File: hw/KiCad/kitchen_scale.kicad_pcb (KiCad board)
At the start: 2 copper layers, 59 x 50 mm, 11 parts, among them J1 Conn_01x08_Socket, J2 Conn_HX711, SW1 SW_Push, SW2 SW_SPST, SW3 SW_Push, SW4 SW_Push, U1 DEBO1_3_7LI_1_0A charge_contr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, U2 WeMos_D1_mini, U3 LF33_TO220

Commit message: Update of fine placement
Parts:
- moved R1 5.59 mm to (82.7, 83.0)
- moved SW1 1.00 mm to (66.8, 115.5)
- moved SW3 1.00 mm to (83.8, 115.5)
- moved SW4 1.00 mm to (100.8, 115.5)
- moved U2 1.00 mm to (116.9, 102.0)
- moved J2 0.80 mm to (79.0, 77.0)
- moved J1 0.50 mm to (64.0, 79.5)
- moved U1 0.50 mm to (60.8, 92.5)
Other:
- board size 59 x 50 mm -> 60 x 50 mm
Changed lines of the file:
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@@
   (net 22 "unconnected-(U2-TX-Pad16)")
   (footprint "Button_Switch_THT:SW_PUSH-12mm" (layer "F.Cu")
-    (at 65.76 115.5)
+    (at 66.76 115.5)
     (descr "SW PUSH 12mm https://www.e-switch.com/system/asset/product_line/data_sheet/143/TL1100.pdf")
     (tags "tact sw push 12mm")
@@
   )
   (footprint "Connector_PinSocket_2.54mm:PinSocket_1x04_P2.54mm_Vertical" (layer "F.Cu")
-    (at 78.2 76.975 90)
+    (at 79 76.975 90)
     (descr "Through hole straight socket strip, 1x04, 2.54mm pitch, single row (from Kicad 4.0.7), script generated")
     (tags "Through hole socket strip THT 1x04 2.54mm single row")
@@
   )
   (footprint "Button_Switch_THT:SW_PUSH-12mm" (layer "F.Cu")
-    (at 82.76 115.5)
+    (at 83.76 115.5)
     (descr "SW PUSH 12mm https://www.e-switch.com/system/asset/product_line/data_sheet/143/TL1100.pdf")
     (tags "tact sw push 12mm")
@@
   )
   (footprint "Resistor_THT:R_Axial_DIN0207_L6.3mm_D2.5mm_P7.62mm_Horizontal" (layer "F.Cu")
-    (at 77.19 82)
+    (at 82.69 83)
     (descr "Resistor, Axial_DIN0207 series, Axial, Horizontal, pin pitch=7.62mm, 0.25W = 1/4W, length*diameter=6.3*2.5mm^2, http://cdn-reichelt.de/documents/datenblatt/B400/1_4W%23YAG.pdf")
     (tags "Resistor Axial_DIN0207 series Axial Horizontal pin pitch 7.62mm 0.25W = 1/4W length 6.3mm diameter 2.5mm")
@@
   )
   (footprint "Mine:DEBO1_3_7LI_1_0A_charge_controller" (layer "F.Cu")
-    (at 61.3 92.5)
+    (at 60.8 92.5)
     (descr "Texas Instruments EUS 5 Pin Double Sided Module")
     (tags "module pcb")
@@
   )
   (footprint "Module:WEMOS_D1_mini_light" (layer "F.Cu")
-    (at 115.86 102 180)
+    (at 116.86 102 180)
     (descr "16-pin module, column spacing 22.86 mm (900 mils), https://wiki.wemos.cc/products:d1:d1_mini, https://c1.staticflickr.com/1/734/31400410271_f278b087db_z.jpg")
     (tags "ESP8266 WiFi microcontroller")
@@
   )
   (footprint "Connector_PinHeader_2.54mm:PinHeader_2x04_P2.54mm_Vertical" (layer "F.Cu")
-    (at 64.46 79.54 90)
+    (at 63.96 79.5 90)
     (descr "Through hole straight pin header, 2x04, 2.54mm pitch, double rows")
     (tags "Through hole pin header THT 2x04 2.54mm double row")
@@
   )
   (footprint "Button_Switch_THT:SW_PUSH-12mm" (layer "F.Cu")
-    (at 99.76 115.5)
+    (at 100.76 115.5)
     (descr "SW PUSH 12mm https://www.e-switch.com/system/asset/product_line/data_sheet/143/TL1100.pdf")
     (tags "tact sw push 12mm")
@@
     )
   )
-  (gr_rect (start 60 75) (end 119 125)
+  (gr_rect (start 60 75) (end 120 125)
     (stroke (width 0.1) (type default)) (fill none) (layer "Edge.Cuts"))
 )

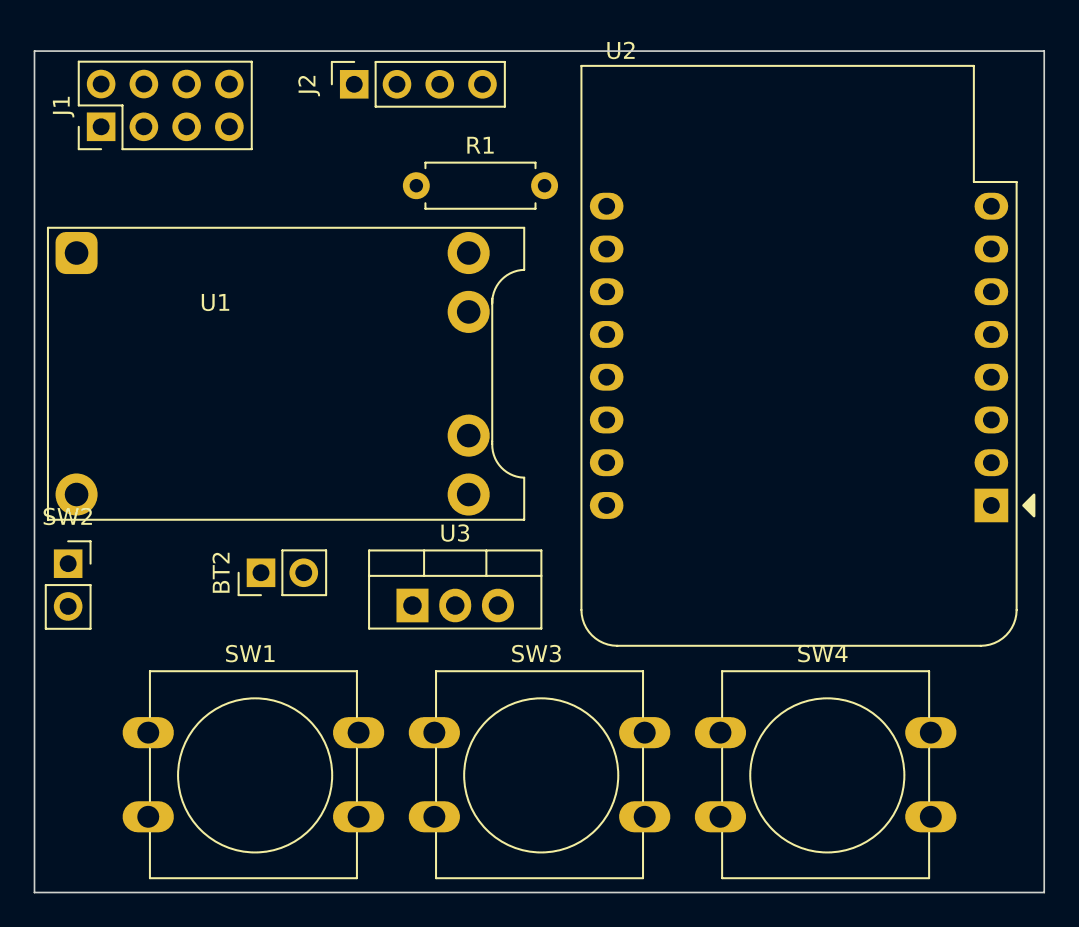
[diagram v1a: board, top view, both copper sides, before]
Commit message: Completed wiring
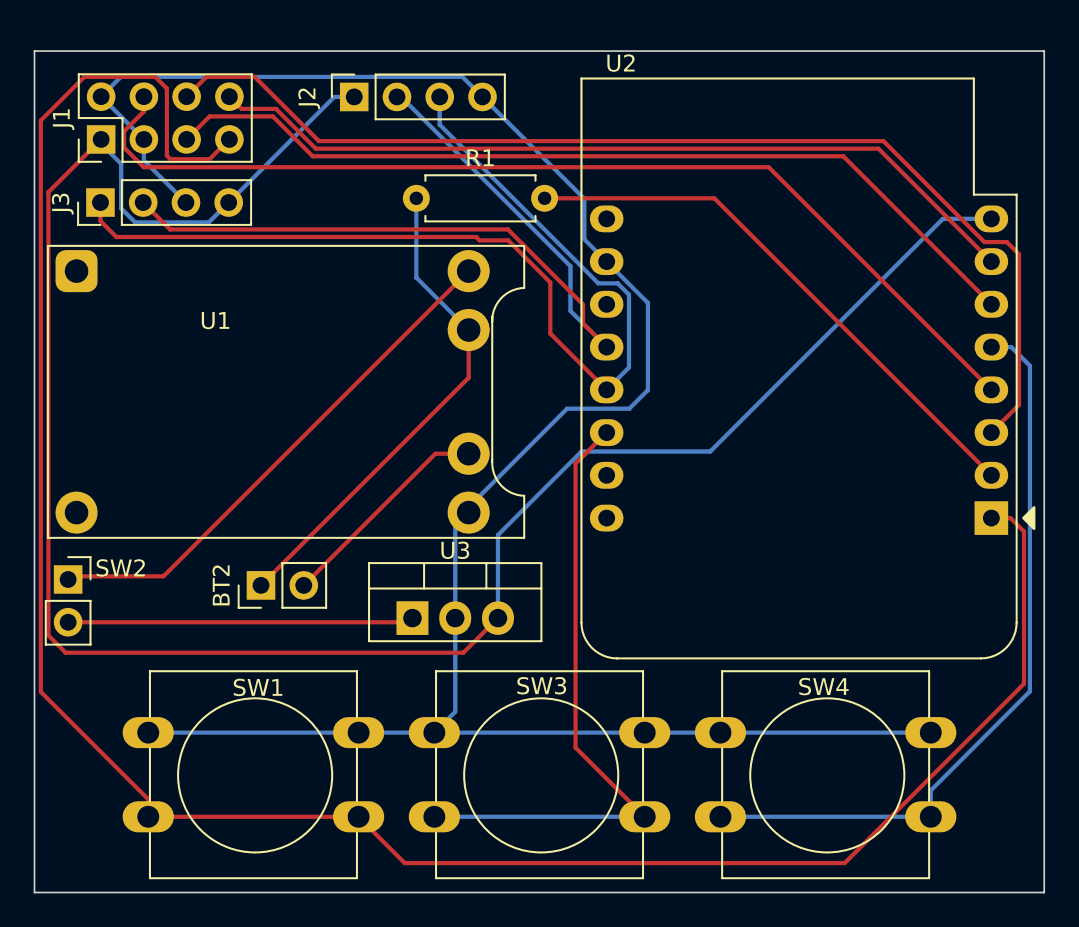
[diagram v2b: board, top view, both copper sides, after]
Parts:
- added J3: Conn_01x04_Pin, Connector_PinHeader_2.54mm:PinHeader_1x04_P2.54mm_Vertical, F.Cu at (63.9, 84.0)
- moved U1 1.08 mm to (60.8, 93.6)
- moved SW2 0.94 mm to (62.0, 106.4)
- moved BT2 0.75 mm to (73.5, 106.8)
- moved J1 0.75 mm to (64.0, 80.2)
- moved J2 0.75 mm to (79.0, 77.7)
- moved R1 0.75 mm to (82.7, 83.8)
- moved U2 0.75 mm to (116.9, 102.8)
- moved U3 0.75 mm to (82.5, 108.7)
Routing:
- net /~{RESET}: track 0.00 -> 130.1 mm
- net GND: track 0.00 -> 128.5 mm
- net +3.3V: track 0.00 -> 122.7 mm
- net /TFT_RS: track 0.00 -> 65.6 mm
- net /SPI_SCK: track 0.00 -> 61.0 mm
- net /D2_DT: track 0.00 -> 60.4 mm
- net /SPI_COPI: track 0.00 -> 53.0 mm
- net /D3_SCK: track 0.00 -> 51.9 mm
- net /SPI_CS: track 0.00 -> 49.3 mm
- net /BTN_2ND: track 0.00 -> 44.5 mm
- net /BTN_TARE: track 0.00 -> 37.8 mm
- net Net-(U2-A0): track 0.00 -> 33.4 mm
- net Net-(SW2-A): track 0.00 -> 31.7 mm
- net +BATT: track 0.00 -> 29.4 mm
- net Net-(SW2-B): track 0.00 -> 20.8 mm
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
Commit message: Add label
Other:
- board text added: "Kitchen Scale 2.0 egsoft, 2025"
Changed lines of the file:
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@@
   (gr_rect (start 60 75) (end 120 125)
     (stroke (width 0.1) (type default)) (fill none) (layer "Edge.Cuts"))
+  (gr_text "Kitchen Scale 2.0\negsoft, 2025" (at 63.15 95.35) (layer "F.SilkS")
+    (effects (font (size 1 1) (thickness 0.15)) (justify left bottom))
+  )
   (segment (start 85.8 91.575) (end 85.8 94.41) (width 0.25) (layer "F.Cu") (net 1))
   (segment (start 85.8 94.41) (end 73.46 106.75) (width 0.25) (layer "F.Cu") (net 1))

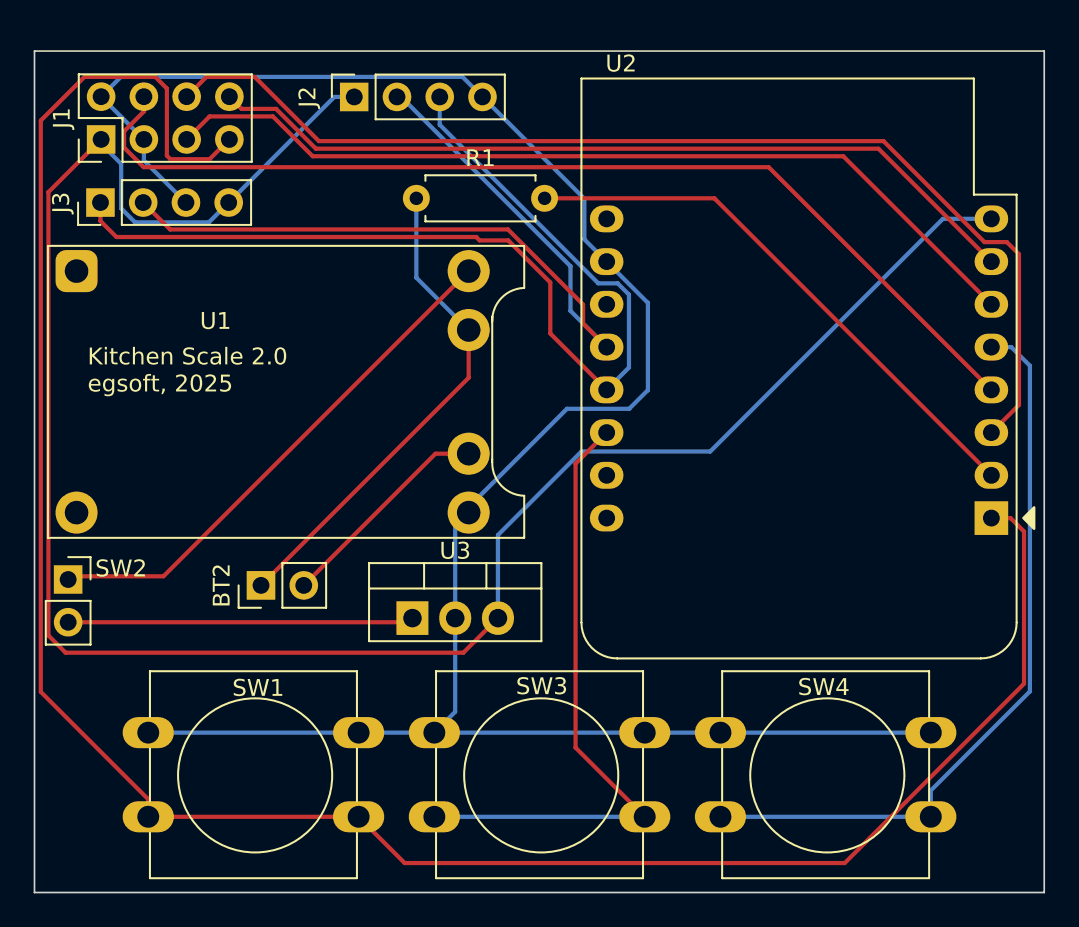
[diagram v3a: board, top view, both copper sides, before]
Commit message: improved routing
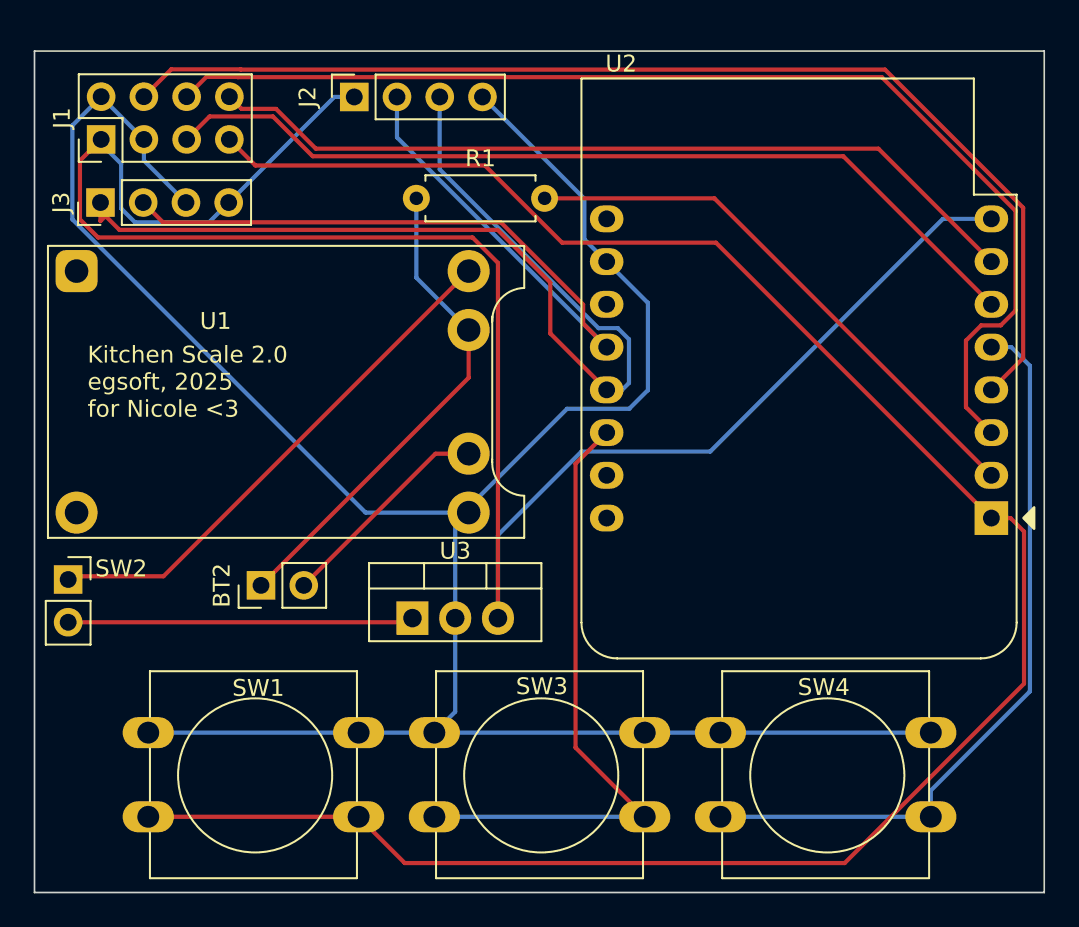
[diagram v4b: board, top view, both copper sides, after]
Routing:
- net GND: track 128.5 -> 143.7 mm
- net /SPI_SCK: track 61.0 -> 67.9 mm
- net /~{RESET}: track 130.1 -> 123.5 mm
- net +3.3V: track 122.7 -> 116.2 mm
- net /TFT_RS: track 65.6 -> 68.7 mm
- net /D2_DT: track 60.4 -> 61.2 mm
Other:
- board text added: "Kitchen Scale 2.0 egsoft, 2025 for Nicole <3"
- board text removed: "Kitchen Scale 2.0 egsoft, 2025"
